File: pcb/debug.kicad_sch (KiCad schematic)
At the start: 1 part

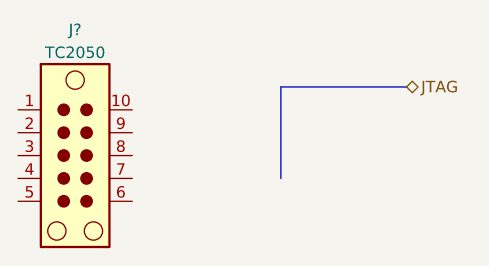
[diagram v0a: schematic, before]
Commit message: addl. updates to power hierarchy
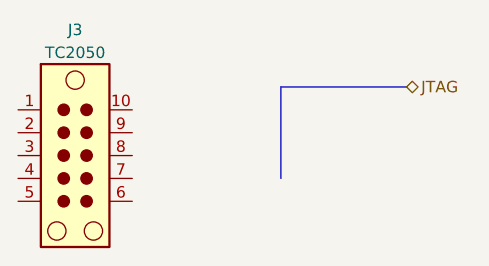
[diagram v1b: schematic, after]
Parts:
- gave numbers to parts that had none: 1
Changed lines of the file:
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@@
 		(dnp no)
 		(fields_autoplaced yes)
-		(property "Reference" "J?"
+		(property "Reference" "J3"
 			(at 69.85 46.99 0)
 			(effects
@@
 			(project "RPi-HwAB-1"
 				(path "/e63e39d7-6ac0-4ffd-8aa3-1841a4541b55/4724a5b2-6700-4a69-acba-b4af3dff5289"
-					(reference "J?")
+					(reference "J3")
 					(unit 1)
 				)

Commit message: added power sequencing through raspi gpio
additionally defined sensors
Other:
- company: (none) -> Andre S Winkel
- title: (none) -> RPi HwAB HAT+
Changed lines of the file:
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@@
 	(generator_version "9.0")
 	(paper "A4")
+	(title_block
+		(title "RPi HwAB HAT+")
+		(date "2025-08-23")
+		(rev "01")
+		(company "Andre S Winkel")
+	)
 	(bus
 		(pts
